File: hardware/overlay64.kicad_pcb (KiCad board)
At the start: 2 copper layers, 44.5 x 58.4 mm, 30 parts, among them IC1 ATMEGA1284, P1 USB, P2 INPUT, P3 CONTROL, P4 MAIN, P5 HOLE, P6 HOLE, P7 HOLE, P8 HOLE, P9 BYPASS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

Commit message: Hardware: Removed explicit OE/OR lines, relabeled control lines
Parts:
- D1, D2: value 3.6 -> 3.6V
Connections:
- IC1 pad 18: /C4 -> /C6
- IC1 pad 19: /C5 -> /C7
- IC1 pad 2: /C0 -> /C2
- IC1 pad 20: /~OE -> /C0
- IC1 pad 21: /~OR -> /C1
- IC1 pad 4: /C1 -> /C3
- IC1 pad 7: /C2 -> /C4
- IC1 pad 8: /C3 -> /C5
- P3 pad 1: /C5 -> /C7
- P3 pad 2: /C4 -> /C6
- P3 pad 3: /C3 -> /C5
- P3 pad 4: /C2 -> /C4
- P3 pad 5: /C1 -> /C3
- P3 pad 6: /C0 -> /C2
- P3 pad 7: /~OR -> /C1
- P3 pad 8: /~OE -> /C0
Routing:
- net /C0: track 54.0 -> 3.81 mm
- net /C1: track 47.6 -> 14.3 mm
- net /C7: track 0.00 -> 27.7 mm
- net /C6: track 0.00 -> 25.4 mm
- net /C5: track 27.7 -> 49.0 mm
- net /C4: track 25.4 -> 46.2 mm
- net /~OR: track 14.3 -> 0.00 mm
- net /C2: track 46.2 -> 54.0 mm
- net /~OE: track 3.81 -> 0.00 mm
- net /C3: track 49.0 -> 47.6 mm

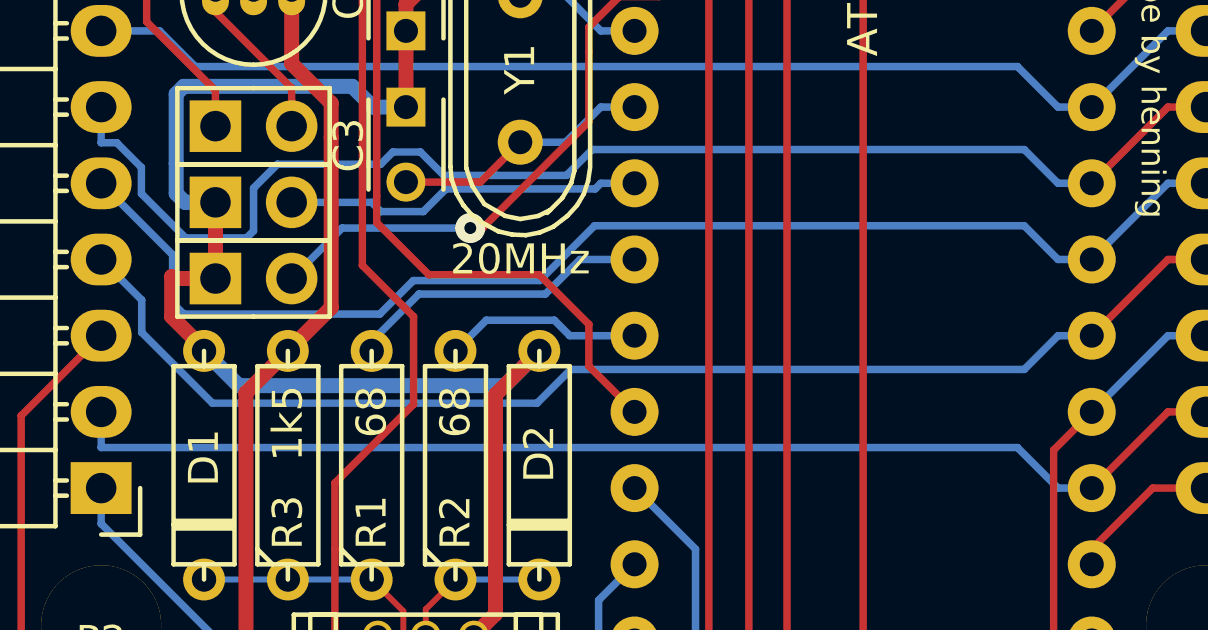
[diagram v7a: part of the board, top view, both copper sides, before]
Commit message: Hardware: Improved USB signal routing
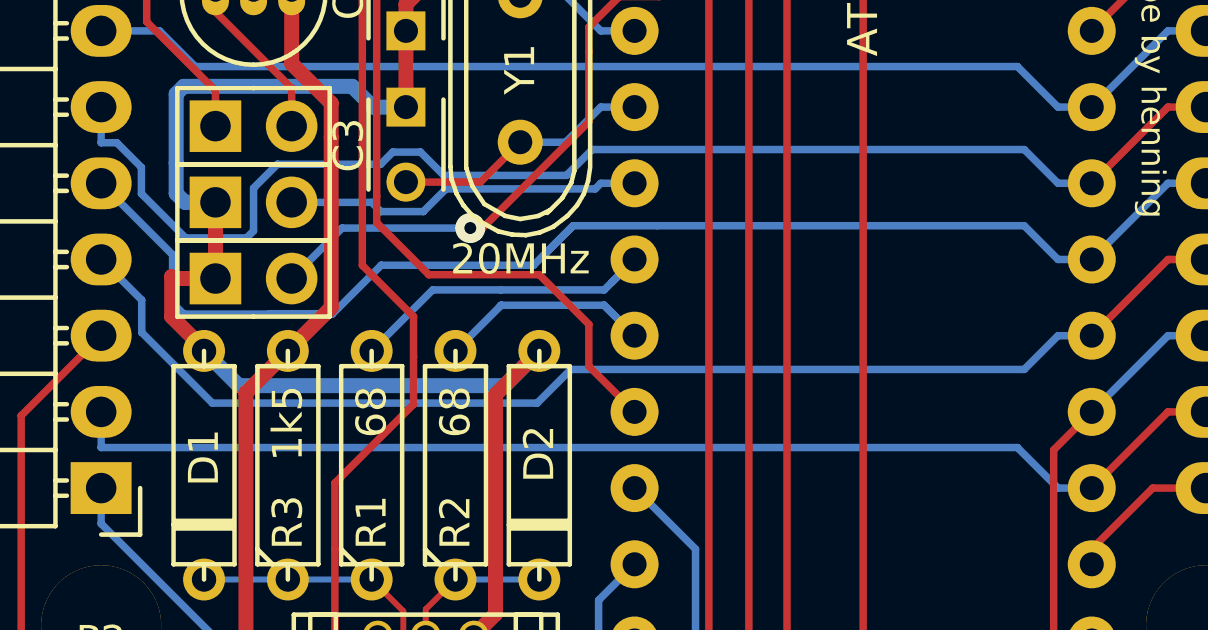
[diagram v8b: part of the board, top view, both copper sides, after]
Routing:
- net /IN11: track 42.3 -> 45.8 mm
- net Net-(IC1-Pad16): track 6.61 -> 8.55 mm
- net Net-(IC1-Pad15): track 10.2 -> 11.1 mm
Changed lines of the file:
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@@
-(kicad_pcb (version 4) (host pcbnew 4.0.3-stable)
+(kicad_pcb (version 4) (host pcbnew 4.0.4-stable)
   (general
-    (links 93)
+    (links 0)
     (no_connects 0)
-    (area 115.494999 60.884999 160.095001 119.455001)
+    (area 92.756429 56.175 190.095 143.035)
     (thickness 1.6)
     (drawings 13)
-    (tracks 436)
+    (tracks 445)
     (zones 0)
     (modules 30)
@@
   (segment (start 132.0209 96.48) (end 129.54 96.48) (width 0.25) (layer F.Cu) (net 4))
   (segment (start 133.35 95.1509) (end 132.0209 96.48) (width 0.25) (layer F.Cu) (net 4))
+  (segment (start 129.794 102.2985) (end 129.794 100.965) (width 0.25) (layer F.Cu) (net 5))
+  (segment (start 129.794 100.965) (end 128.0854 99.2564) (width 0.25) (layer F.Cu) (net 5))
+  (segment (start 128.0854 99.2564) (end 128.0854 85.9096) (width 0.25) (layer F.Cu) (net 5))
+  (segment (start 128.0854 85.9096) (end 130.175 83.82) (width 0.25) (layer F.Cu) (net 5))
   (segment (start 130.175 83.82) (end 130.175 81.915) (width 0.25) (layer F.Cu) (net 5))
   (segment (start 130.175 81.915) (end 125.73 77.47) (width 0.25) (layer F.Cu) (net 5))
   (segment (start 127.1721 108.712) (end 127.1721 106.5079) (width 0.25) (layer F.Cu) (net 5))
-  (segment (start 129.794 100.965) (end 128.0854 99.2564) (width 0.25) (layer F.Cu) (net 5))
-  (segment (start 129.794 103.886) (end 129.794 100.965) (width 0.25) (layer F.Cu) (net 5))
+  (segment (start 129.794 103.886) (end 129.794 102.2985) (width 0.25) (layer F.Cu) (net 5))
   (segment (start 127.1721 106.5079) (end 129.794 103.886) (width 0.25) (layer F.Cu) (net 5))
   (segment (start 130.175 83.82) (end 130.175 81.789398) (width 0.25) (layer F.Cu) (net 5))
   (segment (start 122.936 116.9246) (end 122.0046 116.9246) (width 0.25) (layer F.Cu) (net 5))
   (segment (start 122.0046 116.9246) (end 120.65 115.57) (width 0.25) (layer F.Cu) (net 5))
-  (segment (start 128.0854 85.9096) (end 130.175 83.82) (width 0.25) (layer F.Cu) (net 5))
-  (segment (start 128.0854 99.2564) (end 128.0854 85.9096) (width 0.25) (layer F.Cu) (net 5))
   (segment (start 127.1721 113.9371) (end 127.1721 108.712) (width 0.25) (layer F.Cu) (net 5))
   (segment (start 124.1846 116.9246) (end 127.1721 113.9371) (width 0.25) (layer F.Cu) (net 5))
@@
   (segment (start 130.8774 96.7066) (end 130.1197 97.4643) (width 0.25) (layer B.Cu) (net 19))
   (segment (start 125.73 97.155) (end 126.0393 97.4643) (width 0.25) (layer B.Cu) (net 19))
-  (segment (start 137.16 99.06) (end 135.338298 99.06) (width 0.25) (layer B.Cu) (net 20))
-  (segment (start 134.186296 100.212002) (end 129.972596 100.212002) (width 0.25) (layer B.Cu) (net 20))
-  (segment (start 135.338298 99.06) (end 134.186296 100.212002) (width 0.25) (layer B.Cu) (net 20))
-  (segment (start 128.397 102.108) (end 128.397 101.787598) (width 0.25) (layer B.Cu) (net 20))
-  (segment (start 128.397 101.787598) (end 129.972596 100.212002) (width 0.25) (layer B.Cu) (net 20))
-  (segment (start 137.16 101.6) (end 135.001 101.6) (width 0.25) (layer B.Cu) (net 21))
-  (segment (start 135.001 101.6) (end 134.4851 101.0841) (width 0.25) (layer B.Cu) (net 21))
-  (segment (start 132.2149 101.0841) (end 134.4851 101.0841) (width 0.25) (layer B.Cu) (net 21))
-  (segment (start 131.191 102.108) (end 132.2149 101.0841) (width 0.25) (layer B.Cu) (net 21))
+  (segment (start 132.715 100.076) (end 130.429 100.076) (width 0.25) (layer B.Cu) (net 20))
+  (segment (start 130.429 100.076) (end 128.397 102.108) (width 0.25) (layer B.Cu) (net 20))
+  (segment (start 136.144 100.076) (end 137.16 99.06) (width 0.25) (layer B.Cu) (net 20))
+  (segment (start 132.715 100.076) (end 136.144 100.076) (width 0.25) (layer B.Cu) (net 20))
+  (segment (start 136.398 99.822) (end 137.16 99.06) (width 0.25) (layer B.Cu) (net 20))
+  (segment (start 132.715 100.584) (end 136.144 100.584) (width 0.25) (layer B.Cu) (net 21))
+  (segment (start 136.144 100.584) (end 137.16 101.6) (width 0.25) (layer B.Cu) (net 21))
+  (segment (start 131.191 102.108) (end 132.715 100.584) (width 0.25) (layer B.Cu) (net 21))
+  (segment (start 132.715 100.584) (end 132.6515 100.6475) (width 0.25) (layer B.Cu) (net 21))
+  (segment (start 136.144 100.584) (end 137.16 101.6) (width 0.25) (layer B.Cu) (net 21))
   (segment (start 127.0635 78.0415) (end 127.0635 74.9935) (width 0.25) (layer F.Cu) (net 22))
   (segment (start 127.0635 74.9935) (end 123.19 71.12) (width 0.25) (layer F.Cu) (net 22))
@@
   (segment (start 128.6959 95.885) (end 129.1031 95.4778) (width 0.25) (layer B.Cu) (net 27))
   (segment (start 152.4 96.52) (end 151.2747 96.52) (width 0.25) (layer B.Cu) (net 27))
+  (segment (start 124.968 100.8804) (end 127.0846 100.8804) (width 0.25) (layer B.Cu) (net 28))
+  (segment (start 127.0846 100.8804) (end 128.7145 99.2505) (width 0.25) (layer B.Cu) (net 28))
+  (segment (start 128.7145 99.2505) (end 129.921 99.2505) (width 0.25) (layer B.Cu) (net 28))
+  (segment (start 133.7945 99.2505) (end 135.1103 97.9347) (width 0.25) (layer B.Cu) (net 28))
+  (segment (start 129.921 99.2505) (end 133.7945 99.2505) (width 0.25) (layer B.Cu) (net 28))
+  (segment (start 125.984 100.8804) (end 126.365 100.8804) (width 0.25) (layer B.Cu) (net 28))
+  (segment (start 134.1755 98.8695) (end 135.1103 97.9347) (width 0.25) (layer B.Cu) (net 28))
+  (segment (start 137.922 97.9347) (end 135.1103 97.9347) (width 0.25) (layer B.Cu) (net 28))
+  (segment (start 137.922 97.9347) (end 150.1494 97.9347) (width 0.25) (layer B.Cu) (net 28))
+  (segment (start 152.4 99.06) (end 151.2747 99.06) (width 0.25) (layer B.Cu) (net 28))
+  (segment (start 150.1494 97.9347) (end 151.2747 99.06) (width 0.25) (layer B.Cu) (net 28))
   (segment (start 121.7617 99.949) (end 121.7617 98.9017) (width 0.25) (layer B.Cu) (net 28))
+  (segment (start 122.1327 100.8804) (end 124.968 100.8804) (width 0.25) (layer B.Cu) (net 28))
+  (segment (start 124.968 100.8804) (end 125.984 100.8804) (width 0.25) (layer B.Cu) (net 28))
+  (segment (start 126.365 100.8804) (end 127.0846 100.8804) (width 0.25) (layer B.Cu) (net 28))
+  (segment (start 121.7617 100.5094) (end 122.1327 100.8804) (width 0.25) (layer B.Cu) (net 28))
+  (segment (start 121.7617 99.949) (end 121.7617 100.5094) (width 0.25) (layer B.Cu) (net 28))
   (segment (start 121.7617 98.9017) (end 119.38 96.52) (width 0.25) (layer B.Cu) (net 28))
   (segment (start 156.21 96.52) (end 154.94 96.52) (width 0.25) (layer B.Cu) (net 28))
   (segment (start 154.94 96.52) (end 152.4 99.06) (width 0.25) (layer B.Cu) (net 28))
-  (segment (start 150.1494 97.9347) (end 151.2747 99.06) (width 0.25) (layer B.Cu) (net 28))
-  (segment (start 152.4 99.06) (end 151.2747 99.06) (width 0.25) (layer B.Cu) (net 28))
-  (segment (start 121.7617 99.949) (end 121.7617 100.5094) (width 0.25) (layer B.Cu) (net 28))
-  (segment (start 121.7617 100.5094) (end 122.1327 100.8804) (width 0.25) (layer B.Cu) (net 28))
-  (segment (start 122.1327 100.8804) (end 128.6678 100.8804) (width 0.25) (layer B.Cu) (net 28))
-  (segment (start 128.6678 100.8804) (end 129.7862 99.762) (width 0.25) (layer B.Cu) (net 28))
-  (segment (start 129.7862 99.762) (end 133.9999 99.762) (width 0.25) (layer B.Cu) (net 28))
-  (segment (start 133.9999 99.762) (end 135.8272 97.9347) (width 0.25) (layer B.Cu) (net 28))
-  (segment (start 135.8272 97.9347) (end 150.1494 97.9347) (width 0.25) (layer B.Cu) (net 28))
   (segment (start 120.731 101.473) (end 120.731 100.411) (width 0.25) (layer B.Cu) (net 29))
   (segment (start 120.731 100.411) (end 119.38 99.06) (width 0.25) (layer B.Cu) (net 29))
